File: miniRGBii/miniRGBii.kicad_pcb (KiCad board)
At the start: 2 copper layers, 30 x 15 mm, 28 parts, among them J1 Conn_01x01_Male, J2 Conn_01x01_Male, J3 Conn_01x01_Male, J4 Conn_01x01_Male, J5 Conn_01x01_Male, J6 Conn_01x01_Male, J7 Conn_01x01_Male, J8 Conn_01x01_Male, J9 Conn_01x01_Male

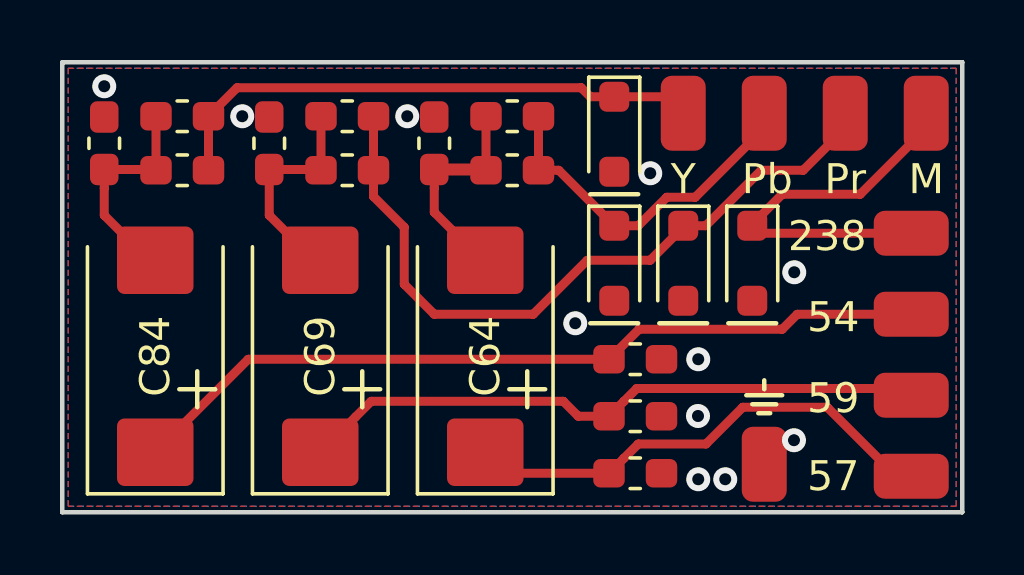
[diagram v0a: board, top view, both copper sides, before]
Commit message: added images folder for people without KiCAD and made curved edges
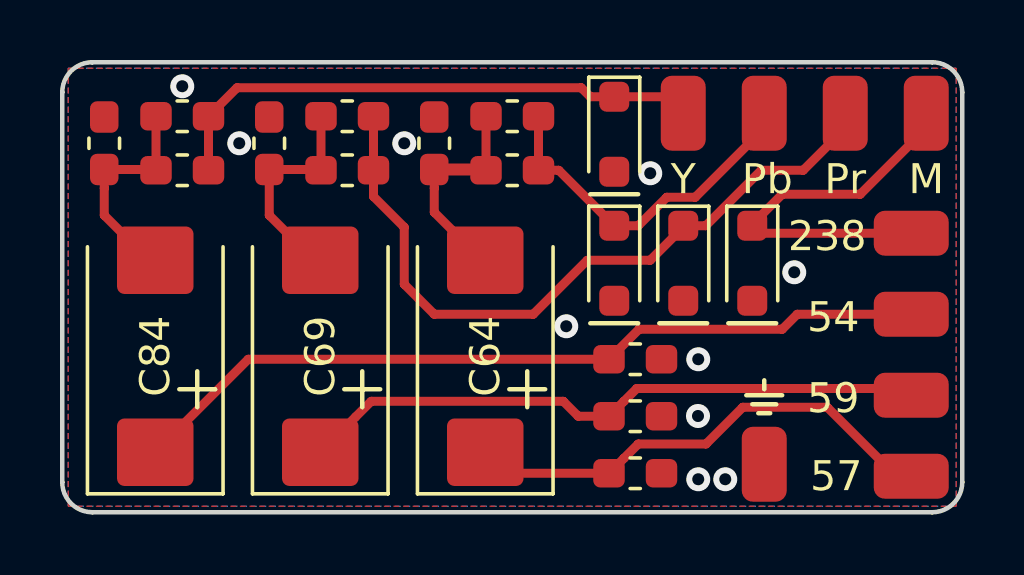
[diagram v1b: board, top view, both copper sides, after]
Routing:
- net GND: vias 11 -> 10
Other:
- outline, holes or cut-outs redrawn
- board text added: "consolebytes.com/miniRGBii"
- board text removed: "consolebytes.com/index.php/ community/postid/37/"
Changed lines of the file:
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@@
   (general
     (thickness 1.6)
-    (drawings 29)
-    (tracks 95)
+    (drawings 33)
+    (tracks 94)
     (zones 0)
     (modules 28)
@@
   (layers
     (0 F.Cu signal)
-    (31 B.Cu signal hide)
+    (31 B.Cu signal)
     (32 B.Adhes user hide)
     (33 F.Adhes user hide)
@@
     (36 B.SilkS user)
     (37 F.SilkS user)
-    (38 B.Mask user hide)
-    (39 F.Mask user hide)
-    (40 Dwgs.User user)
-    (41 Cmts.User user)
-    (42 Eco1.User user)
-    (43 Eco2.User user)
+    (38 B.Mask user)
+    (39 F.Mask user)
+    (40 Dwgs.User user hide)
+    (41 Cmts.User user hide)
+    (42 Eco1.User user hide)
+    (43 Eco2.User user hide)
     (44 Edge.Cuts user)
-    (45 Margin user)
-    (46 B.CrtYd user)
-    (47 F.CrtYd user)
-    (48 B.Fab user)
-    (49 F.Fab user)
+    (45 Margin user hide)
+    (46 B.CrtYd user hide)
+    (47 F.CrtYd user hide)
+    (48 B.Fab user hide)
+    (49 F.Fab user hide)
   )
   (setup
@@
     (visible_elements FFFFFF7F)
     (pcbplotparams
-      (layerselection 0x00010_7ffffffe)
+      (layerselection 0x010f0_ffffffff)
       (usegerberextensions false)
       (usegerberattributes false)
@@
       (padsonsilk false)
       (subtractmaskfromsilk false)
-      (outputformat 4)
+      (outputformat 1)
       (mirror false)
       (drillshape 0)
@@
     )
   )
-  (gr_text "consolebytes.com/index.php/\ncommunity/postid/37/" (at 212.725 66.04) (layer B.SilkS)
+  (gr_line (start 183 68) (end 183 55) (layer Edge.Cuts) (width 0.15))
+  (gr_line (start 212 69) (end 184 69) (layer Edge.Cuts) (width 0.15))
+  (gr_line (start 213 55) (end 213 68) (layer Edge.Cuts) (width 0.15))
+  (gr_line (start 184 54) (end 212 54) (layer Edge.Cuts) (width 0.15))
+  (gr_arc (start 212 68) (end 212 69) (angle -90) (layer Edge.Cuts) (width 0.15))
+  (gr_arc (start 212 55) (end 213 55) (angle -90) (layer Edge.Cuts) (width 0.15))
+  (gr_arc (start 184 68) (end 183 68) (angle -90) (layer Edge.Cuts) (width 0.15))
+  (gr_arc (start 184 55) (end 184 54) (angle -90) (layer Edge.Cuts) (width 0.15))
+  (gr_text consolebytes.com/miniRGBii (at 212.4 66.6) (layer B.SilkS)
     (effects (font (size 1 1) (thickness 0.15)) (justify left mirror))
   )
@@
     (effects (font (size 1.5 1.5) (thickness 0.3)) (justify mirror))
   )
-  (gr_text "by Job#3556 &\nCommandblock6417" (at 212.725 60.96) (layer B.SilkS)
+  (gr_text "by Job#3556 &\nCommandblock6417" (at 212.4 60.4) (layer B.SilkS)
     (effects (font (size 1.5 1.5) (thickness 0.3)) (justify left mirror))
   )
@@
     (effects (font (size 1 1) (thickness 0.25)))
   )
-  (gr_text 57 (at 208.7 67.8) (layer F.SilkS)
+  (gr_text 57 (at 208.8 67.8) (layer F.SilkS)
     (effects (font (size 1 1) (thickness 0.25)))
   )
@@
     (effects (font (size 1 1) (thickness 0.25)))
   )
-  (gr_line (start 213 54) (end 183 54) (layer Edge.Cuts) (width 0.15))
-  (gr_line (start 213 69) (end 213 54) (layer Edge.Cuts) (width 0.15))
-  (gr_line (start 183 69) (end 213 69) (layer Edge.Cuts) (width 0.15))
-  (gr_line (start 183 54) (end 183 69) (layer Edge.Cuts) (width 0.15))
   (segment (start 198.875 55.8) (end 198.875 57.6) (width 0.3) (layer F.Cu) (net 1))
   (segment (start 201.4 59.425) (end 201.4 59.45) (width 0.3) (layer F.Cu) (net 1))
@@
   (segment (start 195.4 59) (end 195.4 58.2) (width 0.3) (layer F.Cu) (net 9))
   (segment (start 197.125 57.6) (end 197.125 55.8) (width 0.3) (layer F.Cu) (net 9))
-  (via (at 200.1 62.7) (size 0.8) (drill 0.4) (layers F.Cu B.Cu) (net 10))
+  (via (at 199.8 62.8) (size 0.8) (drill 0.4) (layers F.Cu B.Cu) (net 10))
   (via (at 207.4 61) (size 0.8) (drill 0.4) (layers F.Cu B.Cu) (net 10))
   (via (at 205.1 67.9) (size 0.8) (drill 0.4) (layers F.Cu B.Cu) (net 10))
-  (via (at 207.391 66.5988) (size 0.8) (drill 0.4) (layers F.Cu B.Cu) (net 10))
   (via (at 202.6 57.7) (size 0.8) (drill 0.4) (layers F.Cu B.Cu) (net 10))
   (via (at 204.2 63.9) (size 0.8) (drill 0.4) (layers F.Cu B.Cu) (net 10))
-  (via (at 184.4 54.8) (size 0.8) (drill 0.4) (layers F.Cu B.Cu) (net 10))
-  (via (at 189 55.8) (size 0.8) (drill 0.4) (layers F.Cu B.Cu) (net 10))
-  (via (at 194.5 55.8) (size 0.8) (drill 0.4) (layers F.Cu B.Cu) (net 10))
+  (via (at 187 54.8) (size 0.8) (drill 0.4) (layers F.Cu B.Cu) (net 10))
+  (via (at 188.9 56.7) (size 0.8) (drill 0.4) (layers F.Cu B.Cu) (net 10))
+  (via (at 194.4 56.7) (size 0.8) (drill 0.4) (layers F.Cu B.Cu) (net 10))
   (via (at 204.190953 65.790953) (size 0.8) (drill 0.4) (layers F.Cu B.Cu) (net 10))
   (via (at 204.2 67.9) (size 0.8) (drill 0.4) (layers F.Cu B.Cu) (net 10))
@@
   (segment (start 206 59.45) (end 206 59.4) (width 0.3) (layer F.Cu) (net 11))
   (segment (start 206 59.4) (end 206.99999 58.40001) (width 0.3) (layer F.Cu) (net 11))
+  (zone (net 10) (net_name GND) (layer B.Cu) (hatch full 0.508)
+    (connect_pads thru_hole_only (clearance 0.3))
+    (min_thickness 0.3)
+    (fill yes (arc_segments 16) (thermal_gap 0.5) (thermal_bridge_width 0.5))
+    (polygon
+      (pts
+        (xy 183.2 54.2) (xy 183.2 68.8) (xy 212.8 68.8) (xy 212.8 54.2)
+      )
+    )
+  )
+  (zone (net 0) (net_name "") (layer B.Mask) (hatch edge 0.508)
+    (connect_pads (clearance 0.3))
+    (min_thickness 0.254)
+    (fill yes (arc_segments 16) (thermal_gap 0.508) (thermal_bridge_width 0.508))
+    (polygon
+      (pts
+        (xy 183.08 54.08) (xy 183.08 54.09) (xy 183.09 54.09) (xy 183.09 54.08)
+      )
+    )
+  )
   (zone (net 10) (net_name GND) (layer F.Cu) (hatch edge 0.508)
     (connect_pads thru_hole_only (clearance 0.3))
@@
       )
     )
-  )
-  (zone (net 10) (net_name GND) (layer B.Cu) (hatch full 0.508)
-    (connect_pads thru_hole_only (clearance 0.3))
-    (min_thickness 0.3)
-    (fill yes (arc_segments 16) (thermal_gap 0.5) (thermal_bridge_width 0.5))
-    (polygon
-      (pts
-        (xy 183.2 54.2) (xy 183.2 68.8) (xy 212.8 68.8) (xy 212.8 54.2)
-      )
-    )
-  )
-  (zone (net 0) (net_name "") (layer B.Mask) (hatch edge 0.508)
-    (connect_pads (clearance 0.3))
-    (min_thickness 0.254)
-    (fill yes (arc_segments 16) (thermal_gap 0.508) (thermal_bridge_width 0.508))
-    (polygon
-      (pts
-        (xy 183.08 54.08) (xy 183.08 54.09) (xy 183.09 54.09) (xy 183.09 54.08)
-      )
-    )

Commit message: Changed url to lowercase, moved vias around
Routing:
- net (no net): vias 0 -> 1
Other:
- board text added: "consolebytes.com/minirgbii"
- board text removed: "consolebytes.com/miniRGBii"
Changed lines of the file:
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@@
     (thickness 1.6)
     (drawings 33)
-    (tracks 94)
+    (tracks 95)
     (zones 0)
     (modules 28)
@@
   (gr_arc (start 184 68) (end 183 68) (angle -90) (layer Edge.Cuts) (width 0.15))
   (gr_arc (start 184 55) (end 184 54) (angle -90) (layer Edge.Cuts) (width 0.15))
-  (gr_text consolebytes.com/miniRGBii (at 212.4 66.6) (layer B.SilkS)
+  (gr_text consolebytes.com/minirgbii (at 212.4 66.6) (layer B.SilkS)
     (effects (font (size 1 1) (thickness 0.15)) (justify left mirror))
   )
@@
     (effects (font (size 1 1) (thickness 0.25)))
   )
+  (via (at 185 54.8) (size 0.8) (drill 0.4) (layers F.Cu B.Cu) (net 0))
   (segment (start 198.875 55.8) (end 198.875 57.6) (width 0.3) (layer F.Cu) (net 1))
   (segment (start 201.4 59.425) (end 201.4 59.45) (width 0.3) (layer F.Cu) (net 1))
@@
   (segment (start 197.125 57.6) (end 197.125 55.8) (width 0.3) (layer F.Cu) (net 9))
   (via (at 199.8 62.8) (size 0.8) (drill 0.4) (layers F.Cu B.Cu) (net 10))
-  (via (at 207.4 61) (size 0.8) (drill 0.4) (layers F.Cu B.Cu) (net 10))
+  (via (at 205 60.5) (size 0.8) (drill 0.4) (layers F.Cu B.Cu) (net 10))
   (via (at 205.1 67.9) (size 0.8) (drill 0.4) (layers F.Cu B.Cu) (net 10))
   (via (at 202.6 57.7) (size 0.8) (drill 0.4) (layers F.Cu B.Cu) (net 10))

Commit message: finalised (hopefully) the panel version
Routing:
- net GND: vias 10 -> 11
- net (no net): vias 1 -> 0
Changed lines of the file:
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@@
       (padsonsilk false)
       (subtractmaskfromsilk false)
-      (outputformat 1)
+      (outputformat 4)
       (mirror false)
       (drillshape 0)
       (scaleselection 1)
-      (outputdirectory "output/"))
+      (outputdirectory "images/output_layer_images_"))
   )
   (net 0 "")
@@
     (effects (font (size 1 1) (thickness 0.25)))
   )
-  (via (at 185 54.8) (size 0.8) (drill 0.4) (layers F.Cu B.Cu) (net 0))
+  (via (at 185 54.8) (size 0.8) (drill 0.4) (layers F.Cu B.Cu) (net 10))
   (segment (start 198.875 55.8) (end 198.875 57.6) (width 0.3) (layer F.Cu) (net 1))
   (segment (start 201.4 59.425) (end 201.4 59.45) (width 0.3) (layer F.Cu) (net 1))

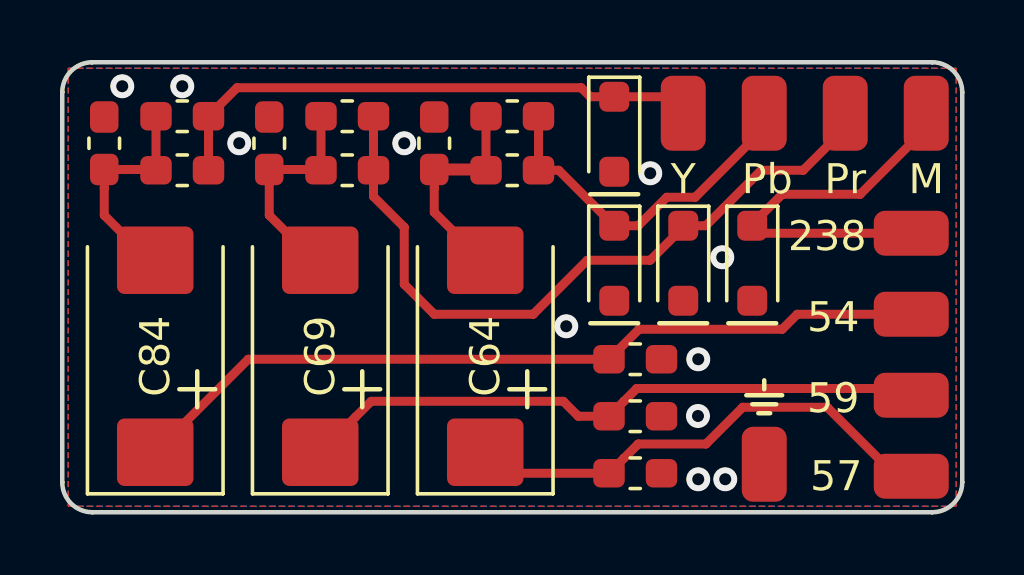
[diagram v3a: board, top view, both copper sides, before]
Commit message: Add Bill Of Materials for miniRGBii
Signed-off-by: Devnol <pgkoutsoumanis@gmail.com>
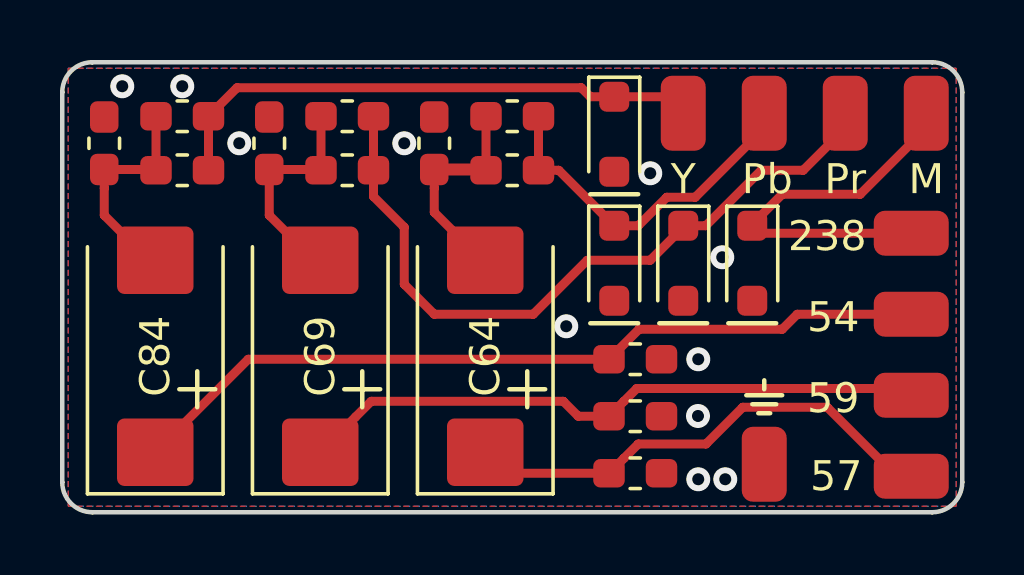
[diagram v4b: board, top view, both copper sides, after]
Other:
- net class Default removed

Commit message: That shouldn't have been removed
Signed-off-by: Devnol <pgkoutsoumanis@gmail.com>
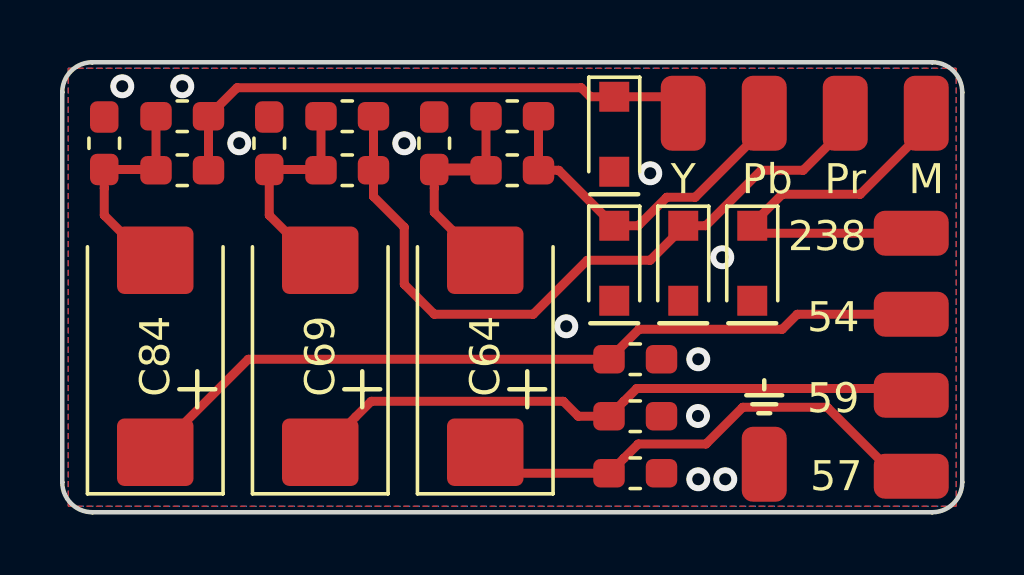
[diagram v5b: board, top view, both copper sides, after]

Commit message: remove miniRGBii_panel, may be added back after update has finished
Signed-off-by: Devnol <pgkoutsoumanis@gmail.com>
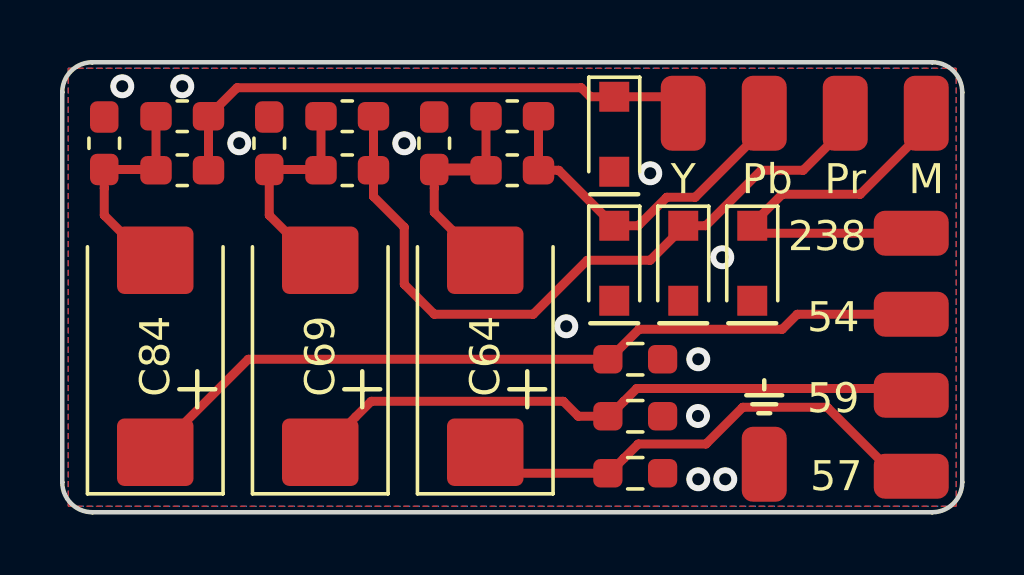
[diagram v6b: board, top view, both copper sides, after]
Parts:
- R37, R39, R40: footprint Resistor_SMD:R_0603_1608Metric_Pad1.05x0.95mm_HandSolder -> Resistor_SMD:R_0603_1608Metric_Pad0.98x0.95mm_HandSolder

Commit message: Fix 3d model directories for KiCAD 6
Signed-off-by: Devnol <pgkoutsoumanis@gmail.com>
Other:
- board text added: "Rev ${REVISION}"
- board text added: "by Job#3556 & Devnol#9366"
- board text added: "discord.gg/7jNHphfDQk"
- board text removed: "by Job#3556 & Commandblock6417"
- board text removed: "consolebytes.com/minirgbii"
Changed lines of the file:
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@@
   (title_block
     (title "miniRGBii PCB Layout")
+    (rev "1.0")
     (company "Wii mini Hacking")
     (comment 1 "Devnol")
@@
     (pad "2" smd roundrect locked (at 0.875 0) (size 1.05 0.95) (layers "F.Cu" "F.Paste" "F.Mask") (roundrect_rratio 0.25)
       (net 6 "PrOut") (pintype "passive"))
-    (model "${KISYS3DMOD}/Capacitor_SMD.3dshapes/C_0603_1608Metric.wrl"
+    (model "${KICAD6_3DMODEL_DIR}/Capacitor_SMD.3dshapes/C_0603_1608Metric.wrl"
       (offset (xyz 0 0 0))
       (scale (xyz 1 1 1))
@@
     (pad "2" smd roundrect locked (at 0.875 0 270) (size 1.05 0.95) (layers "F.Cu" "F.Paste" "F.Mask") (roundrect_rratio 0.25)
       (net 7 "Net-(C66-Pad1)") (pintype "passive"))
-    (model "${KISYS3DMOD}/Capacitor_SMD.3dshapes/C_0603_1608Metric.wrl"
+    (model "${KICAD6_3DMODEL_DIR}/Capacitor_SMD.3dshapes/C_0603_1608Metric.wrl"
       (offset (xyz 0 0 0))
       (scale (xyz 1 1 1))
@@
     (pad "2" smd roundrect locked (at 0.875 0) (size 1.05 0.95) (layers "F.Cu" "F.Paste" "F.Mask") (roundrect_rratio 0.25)
       (net 1 "PbOut") (pintype "passive"))
-    (model "${KISYS3DMOD}/Capacitor_SMD.3dshapes/C_0603_1608Metric.wrl"
+    (model "${KICAD6_3DMODEL_DIR}/Capacitor_SMD.3dshapes/C_0603_1608Metric.wrl"
       (offset (xyz 0 0 0))
       (scale (xyz 1 1 1))
@@
     (pad "2" smd roundrect locked (at 0.875 0 270) (size 1.05 0.95) (layers "F.Cu" "F.Paste" "F.Mask") (roundrect_rratio 0.25)
       (net 9 "Net-(C64-Pad2)") (pintype "passive"))
-    (model "${KISYS3DMOD}/Capacitor_SMD.3dshapes/C_0603_1608Metric.wrl"
+    (model "${KICAD6_3DMODEL_DIR}/Capacitor_SMD.3dshapes/C_0603_1608Metric.wrl"
       (offset (xyz 0 0 0))
       (scale (xyz 1 1 1))
@@
     (pad "2" smd roundrect locked (at 0.875 0) (size 1.05 0.95) (layers "F.Cu" "F.Paste" "F.Mask") (roundrect_rratio 0.25)
       (net 5 "YOut") (pintype "passive"))
-    (model "${KISYS3DMOD}/Capacitor_SMD.3dshapes/C_0603_1608Metric.wrl"
+    (model "${KICAD6_3DMODEL_DIR}/Capacitor_SMD.3dshapes/C_0603_1608Metric.wrl"
       (offset (xyz 0 0 0))
       (scale (xyz 1 1 1))
@@
     (effects (font (size 1.5 1.5) (thickness 0.3)) (justify mirror))
   )
-  (gr_text "by Job#3556 &\nCommandblock6417" (at 212.4 60.4) (layer "B.SilkS")
+  (gr_text "by Job#3556 &\nDevnol#9366" (at 212.4 60.4) (layer "B.SilkS")
     (effects (font (size 1.5 1.5) (thickness 0.3)) (justify left mirror))
   )
-  (gr_text "consolebytes.com/minirgbii" (at 212.4 66.6) (layer "B.SilkS")
+  (gr_text "discord.gg/7jNHphfDQk" (at 212.4 66.6) (layer "B.SilkS")
     (effects (font (size 1 1) (thickness 0.15)) (justify left mirror))
   )
+  (gr_text "Rev ${REVISION}" (at 186.69 67.31) (layer "B.SilkS")
+    (effects (font (size 1 1) (thickness 0.15)) (justify mirror))
+  )
   (gr_text "M" (at 211.8 57.9) (layer "F.SilkS")
